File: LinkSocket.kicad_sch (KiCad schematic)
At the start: 4 parts, among them J201 2x05_Horizontal, U201 THVD24x2

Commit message: Link termination
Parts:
- R201: value 120R -> 100R
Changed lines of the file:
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@@
 			)
 		)
-		(property "Value" "120R"
+		(property "Value" "100R"
 			(at 157.48 119.38 0)
 			(effects

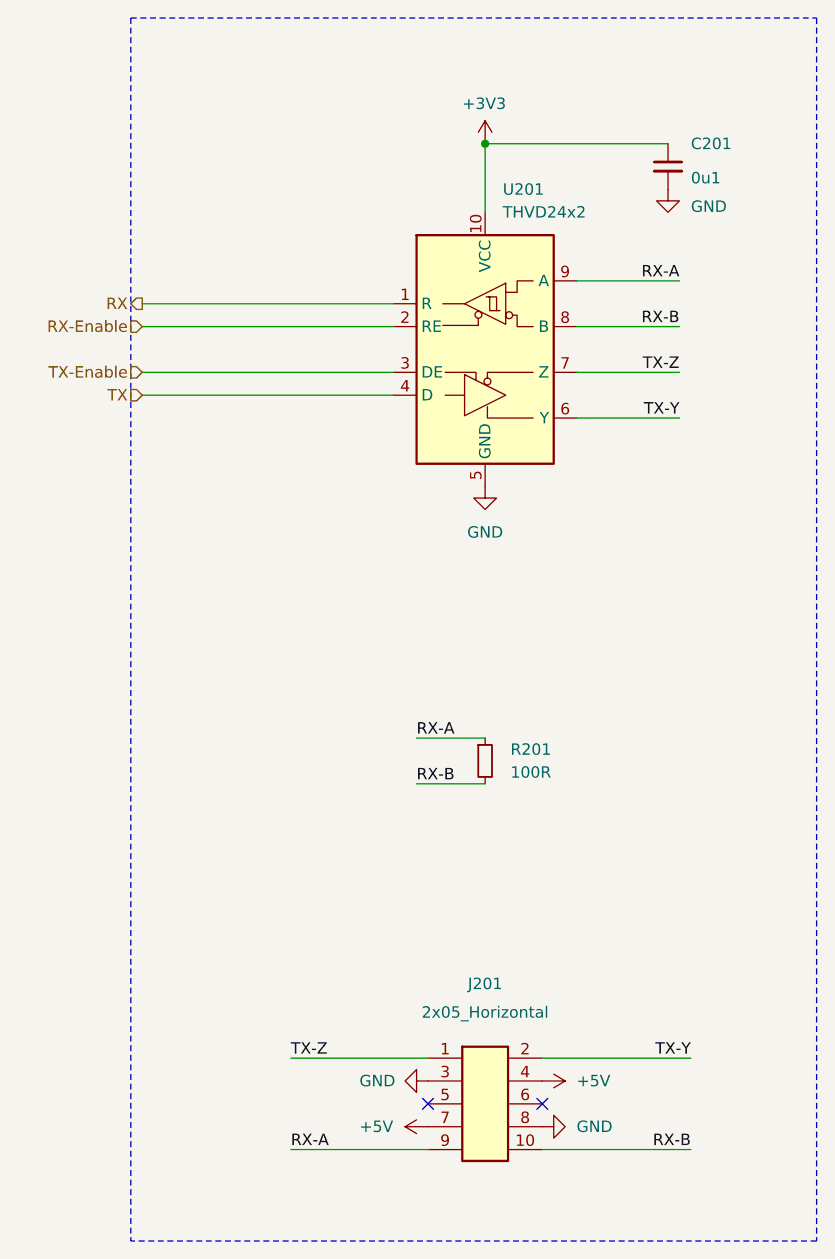
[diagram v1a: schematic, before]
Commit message: Replace Order_Number
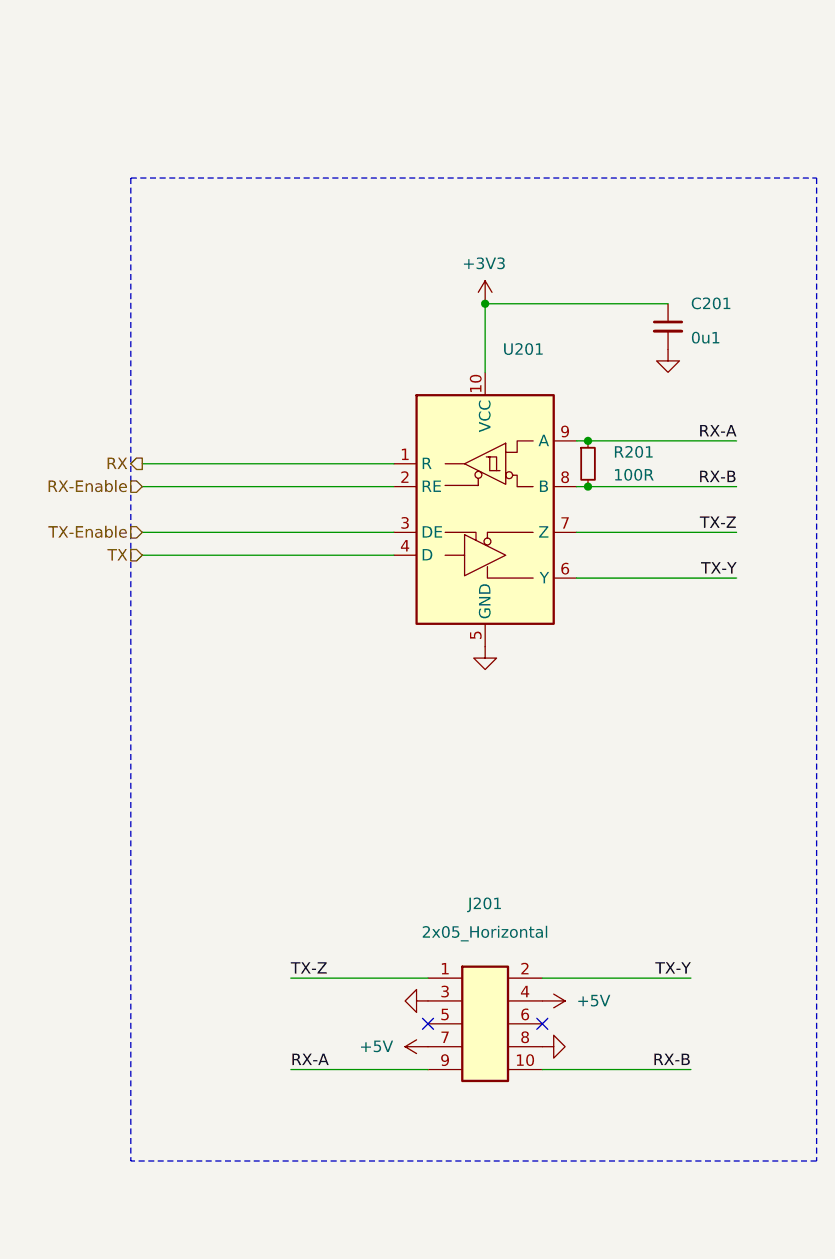
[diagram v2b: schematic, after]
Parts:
- C201: footprint Capacitor_SMD:C_0603_1608Metric -> V2_Capacitor_SMD:C_0603; symbol Device:C_Small -> V2_Device:C_0603_0u1; Manufacturer (none) -> TDK; Mouser (none) -> 810-CGA3E2X7R1H104MA; Product (none) -> CGA3E2X7R1H104M080AA; Rating (none) -> 50V
- J201: Manufacturer (none) -> Amphenol FCI; Mouser (none) -> 649-200211120001T4LF; Product (none) -> 20021112-00010T4LF
- R201: footprint Resistor_SMD:R_0603_1608Metric -> V2_Resistor_SMD:R_0603; symbol Device:R_Small -> V2_Device:R_0603_100R; Manufacturer (none) -> Vishay; Mouser (none) -> 71-CRCW0603100RFKEAH; Product (none) -> CRCW0603100RFKEAHP; Rating (none) -> 330mW
- U201: value THVD24x2 -> (none)
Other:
- moved on the sheet: C201, J201, R201, U201

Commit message: Update Library
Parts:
- C201: symbol V2_Device:C_0603_0u1 -> V2_Capacitor:0603_0u1
- R201: symbol V2_Device:R_0603_100R -> V2_Resistor:0603_100R
- U201: value (none) -> ~
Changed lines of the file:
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@@
 		(on_board yes)
 		(dnp no)
-		(property "Reference" "#PWR0201"
+		(property "Reference" "#PWR201"
 			(at 152.4 71.12 0)
 			(effects
@@
 			(project "control"
 				(path "/6c8448b4-b04d-47e1-934e-e40cbe27a7be/1002ed5a-7984-4d39-a94b-5f1a9a481740"
-					(reference "#PWR0201")
+					(reference "#PWR201")
 					(unit 1)
 				)
@@
 		(on_board yes)
 		(dnp no)
-		(property "Reference" "#PWR0203"
+		(property "Reference" "#PWR203"
 			(at 152.4 111.76 0)
 			(effects
@@
 			(project "control"
 				(path "/6c8448b4-b04d-47e1-934e-e40cbe27a7be/1002ed5a-7984-4d39-a94b-5f1a9a481740"
-					(reference "#PWR0203")
+					(reference "#PWR203")
 					(unit 1)
 				)
@@
 		(dnp no)
 		(fields_autoplaced yes)
-		(property "Reference" "#PWR0202"
+		(property "Reference" "#PWR202"
 			(at 172.72 78.74 0)
 			(effects
@@
 			(project "control"
 				(path "/6c8448b4-b04d-47e1-934e-e40cbe27a7be/1002ed5a-7984-4d39-a94b-5f1a9a481740"
-					(reference "#PWR0202")
+					(reference "#PWR202")
 					(unit 1)
 				)
@@
 			)
 		)
-		(property "Value" ""
+		(property "Value" "~"
 			(at 154.3559 74.93 0)
 			(effects
@@
 	)
 	(symbol
-		(lib_id "V2_Device:R_0603_100R")
+		(lib_id "V2_Resistor:0603_100R")
 		(at 163.83 85.09 0)
 		(unit 1)
@@
 		(on_board yes)
 		(dnp no)
-		(property "Reference" "#PWR0204"
+		(property "Reference" "#PWR204"
 			(at 139.7 144.78 0)
 			(effects
@@
 			(project "control"
 				(path "/6c8448b4-b04d-47e1-934e-e40cbe27a7be/1002ed5a-7984-4d39-a94b-5f1a9a481740"
-					(reference "#PWR0204")
+					(reference "#PWR204")
 					(unit 1)
 				)
@@
 	)
 	(symbol
-		(lib_id "V2_Device:C_0603_0u1")
+		(lib_id "V2_Capacitor:0603_0u1")
 		(at 172.72 69.85 0)
 		(unit 1)
@@
 		(on_board yes)
 		(dnp no)
-		(property "Reference" "#PWR0207"
+		(property "Reference" "#PWR207"
 			(at 165.1 149.86 0)
 			(effects
@@
 			(project "control"
 				(path "/6c8448b4-b04d-47e1-934e-e40cbe27a7be/1002ed5a-7984-4d39-a94b-5f1a9a481740"
-					(reference "#PWR0207")
+					(reference "#PWR207")
 					(unit 1)
 				)
@@
 		(on_board yes)
 		(dnp no)
-		(property "Reference" "#PWR0206"
+		(property "Reference" "#PWR206"
 			(at 149.86 149.86 0)
 			(effects
@@
 			(project "control"
 				(path "/6c8448b4-b04d-47e1-934e-e40cbe27a7be/1002ed5a-7984-4d39-a94b-5f1a9a481740"
-					(reference "#PWR0206")
+					(reference "#PWR206")
 					(unit 1)
 				)
@@
 		(on_board yes)
 		(dnp no)
-		(property "Reference" "#PWR0205"
+		(property "Reference" "#PWR205"
 			(at 154.94 144.78 0)
 			(effects
@@
 			(project "control"
 				(path "/6c8448b4-b04d-47e1-934e-e40cbe27a7be/1002ed5a-7984-4d39-a94b-5f1a9a481740"
-					(reference "#PWR0205")
-					(unit 1)
-				)
+					(reference "#PWR205")
+					(unit 1)
+				)

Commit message: Replace diode
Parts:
- U201: value ~ -> (none)
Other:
- title: V2 Link -> V2 control

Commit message: Good Bye Imperial
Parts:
- C201: footprint V2_Capacitor_SMD:C_0603 -> V2_Capacitor_SMD:C_1608; symbol V2_Capacitor:0603_0u1 -> V2_Capacitor:1608_0u1
- R201: footprint V2_Resistor_SMD:R_0603 -> V2_Resistor_SMD:R_1608; symbol V2_Resistor:0603_100R -> V2_Resistor:1608_100R
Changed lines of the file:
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@@
 	)
 	(symbol
-		(lib_id "V2_Resistor:0603_100R")
+		(lib_id "V2_Resistor:1608_100R")
 		(at 163.83 85.09 0)
 		(unit 1)
@@
 			)
 		)
-		(property "Footprint" "V2_Resistor_SMD:R_0603"
+		(property "Footprint" "V2_Resistor_SMD:R_1608"
 			(at 163.83 100.838 0)
 			(hide yes)
@@
 	)
 	(symbol
-		(lib_id "V2_Capacitor:0603_0u1")
+		(lib_id "V2_Capacitor:1608_0u1")
 		(at 172.72 69.85 0)
 		(unit 1)
@@
 			)
 		)
-		(property "Footprint" "V2_Capacitor_SMD:C_0603"
+		(property "Footprint" "V2_Capacitor_SMD:C_1608"
 			(at 172.72 86.868 0)
 			(hide yes)
